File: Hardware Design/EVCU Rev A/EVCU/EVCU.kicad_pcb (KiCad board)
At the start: 4 copper layers, 119.4 x 76.4 mm, 89 parts, among them J1 Conn_01x06, J2 Conn_01x02, J3 APPS/BSE_Conn, J4 Micro_SD_Card, J5 DB9_Male, J6 Conn_01x02, Q1 Q_PMOS_GSD, U1 AZ1117-3.3, U10 EMIF06-MSD02N16, U11 ESDALC6V1W5, U2 AP62250WU-7, U3 STM32L4R9ZITx, U4 LM358, U5 MPU-6500, U6 SN65HVD230, U7 LM358, U9 ESDCAN24-2BLY, X1 ECS-2520MV-160-CN-TR

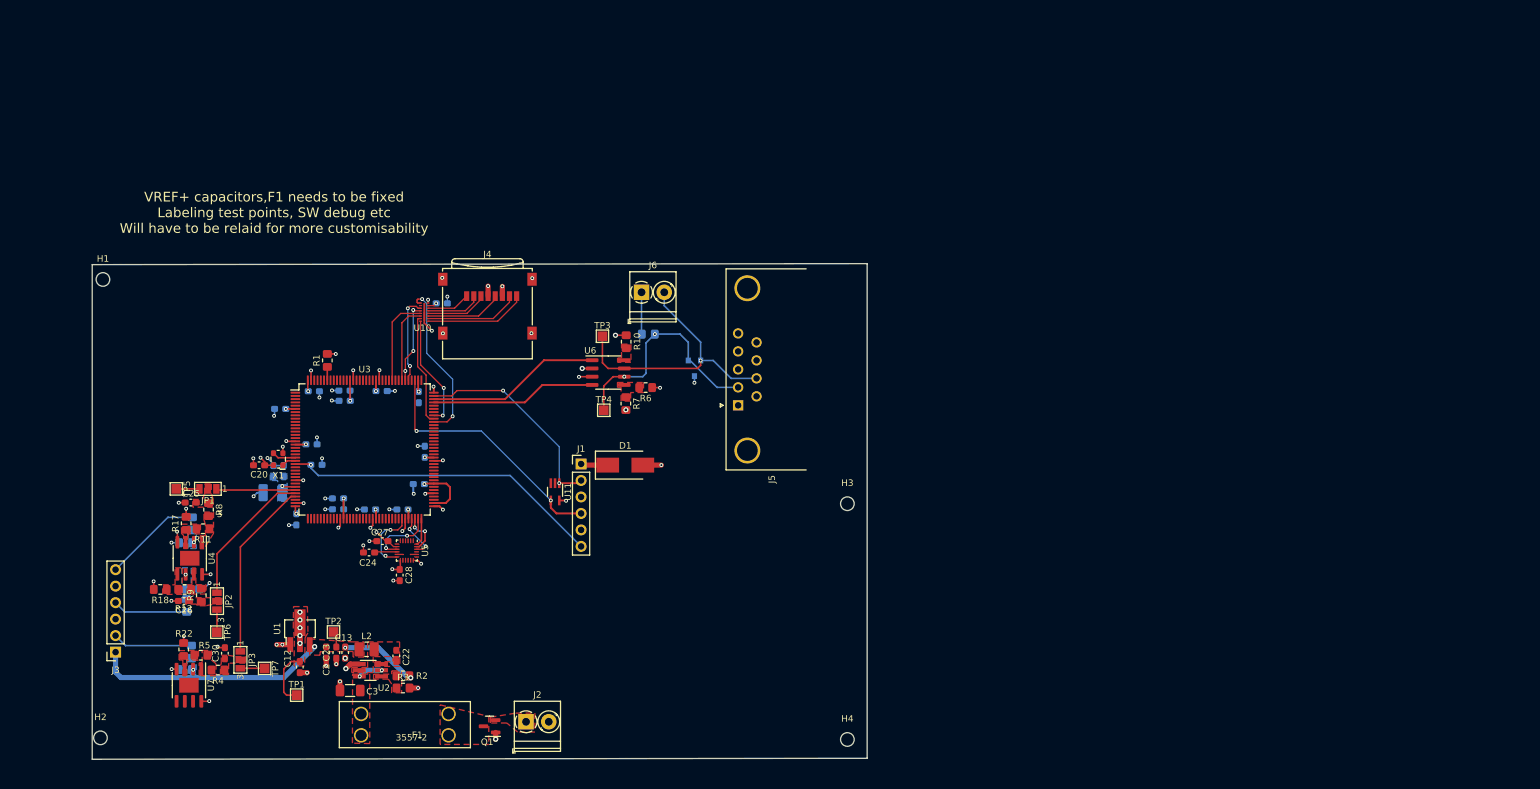
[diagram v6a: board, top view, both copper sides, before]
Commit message: silkscreen and drc clean up
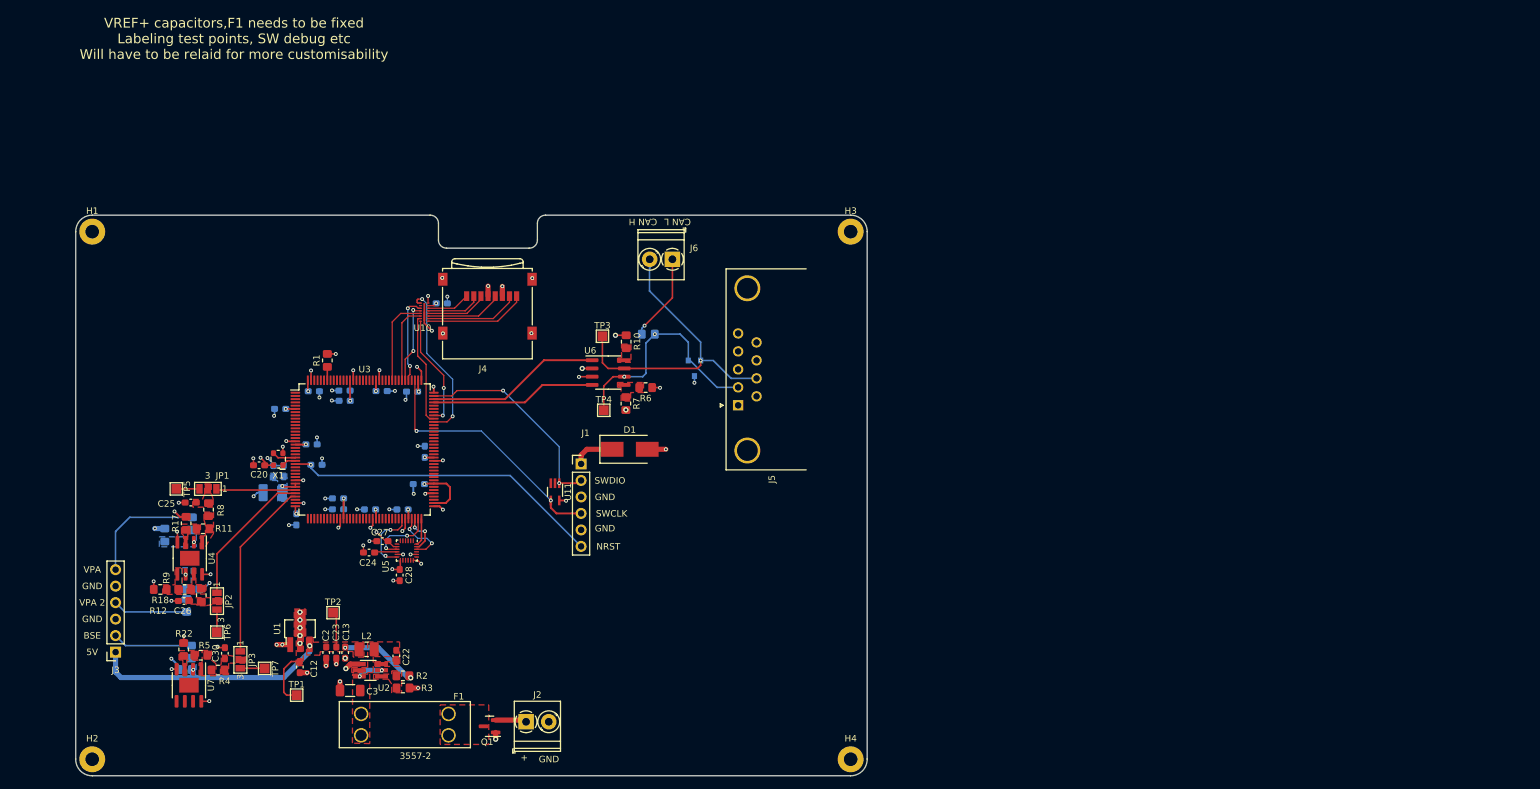
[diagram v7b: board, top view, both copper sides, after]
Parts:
- moved H3 41.9 mm to (132.1, 25.4)
- moved H1 7.55 mm to (15.2, 25.4)
- moved J6 6.96 mm to (104.6, 29.7), turned to 180 degrees
- moved H2 3.54 mm to (15.2, 106.7)
- moved R13 3.43 mm to (26.4, 72.1), turned to 90 degrees
- moved H4 3.09 mm to (132.1, 106.7)
- moved TP2 2.97 mm to (52.3, 84.1)
- moved D1 2.53 mm to (98.0, 58.9)
- moved C16 1.33 mm to (64.5, 50.0), turned to 180 degrees
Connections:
- F1 pad 1: (no net) -> Net-(F1-Pad)
- F1 pad 2: (no net) -> Net-(F1-Pad)
- F1 pad 3: (no net) -> +BATT
- F1 pad 4: (no net) -> +BATT
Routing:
- net Net-(J6-Pad1): track 6.47 -> 13.5 mm, vias 0 -> 1
- net GND: track 83.4 -> 90.3 mm, vias 66 -> 71
- net /CAN_H: track 43.1 -> 49.1 mm
- net Net-(J2-Pad1): track 0.00 -> 4.78 mm
- net /VPA: track 15.2 -> 18.6 mm
- net +3V3: track 59.3 -> 62.3 mm
- net +5V: track 50.6 -> 53.4 mm
- net /ACCEL_CS: track 6.98 -> 8.92 mm
- net +3.3VA: track 2.06 -> 2.56 mm
- net /MCU_DAT3: vias 3 -> 2
- removed copper zone on F.Cu, net Net-(J2-Pad1)
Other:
- board size 119.4 x 76.4 mm -> 121.9 x 86.4 mm
- board text added: "+"
- board text added: "5V"
- board text added: "BSE"
- board text added: "CAN H"
- board text added: "CAN L"
- board text added: "GND"
- board text added: "NRST"
- board text added: "SWCLK"
- board text added: "SWDIO"
- board text added: "VPA"
- board text added: "VPA 2"

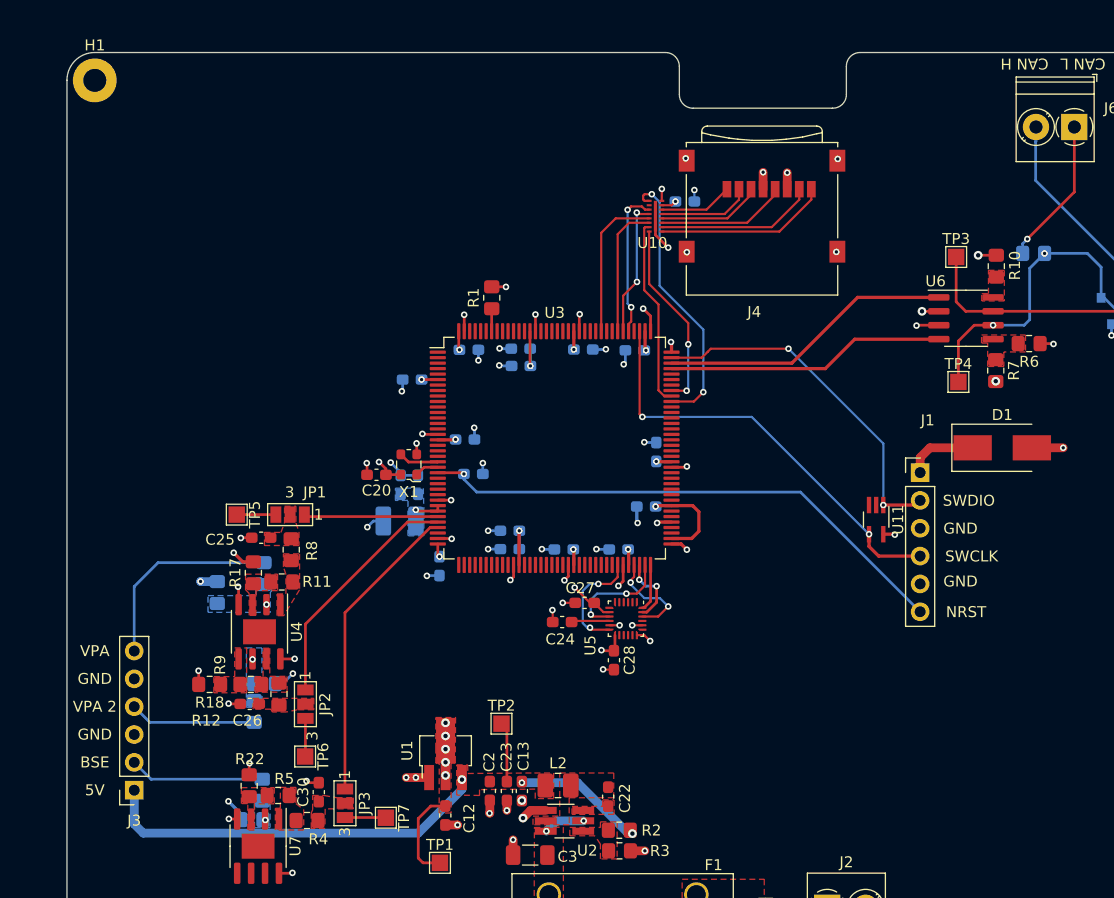
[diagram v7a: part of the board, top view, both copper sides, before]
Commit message: added vref+ caps, fixed f1 via error, fixed gyro footprint, pcb ready for manufacturing
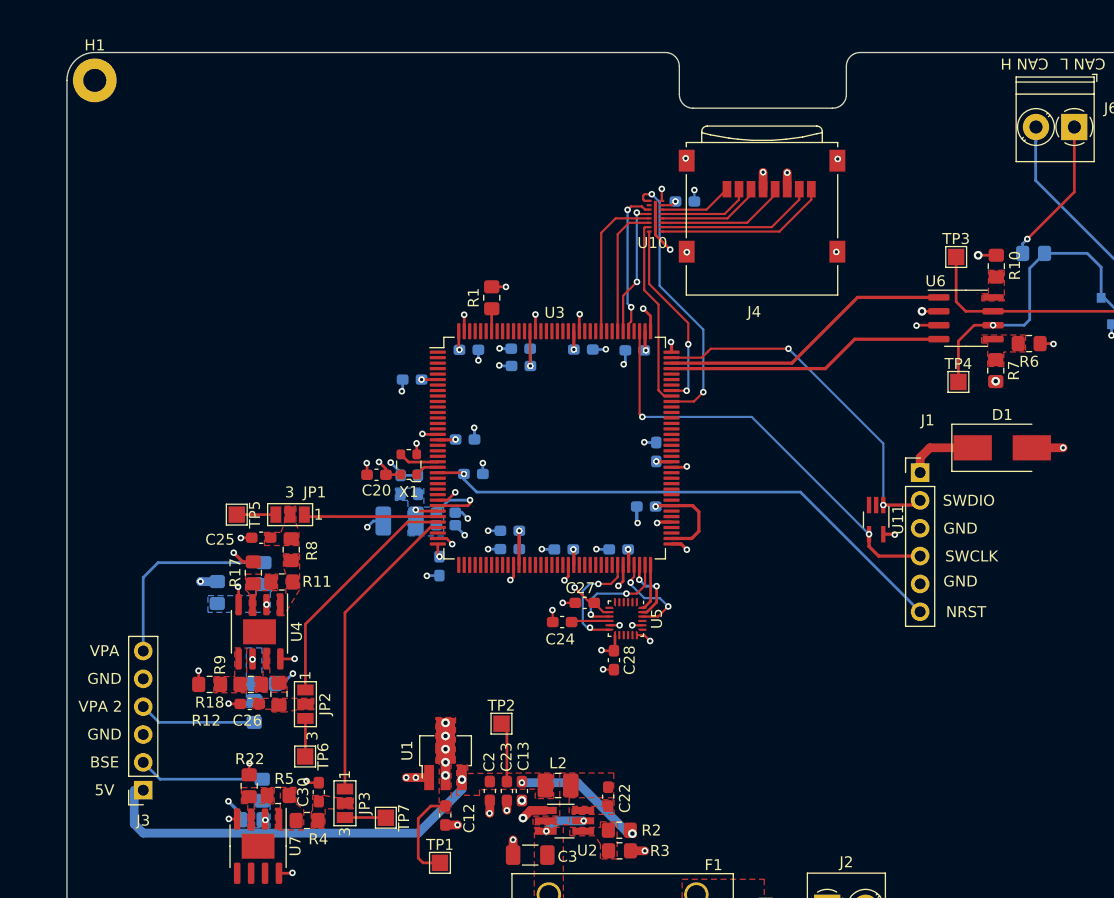
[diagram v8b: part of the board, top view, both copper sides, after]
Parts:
- added C32: 1uF, Capacitor_SMD:C_0603_1608Metric_Pad1.08x0.95mm_HandSolder, B.Cu at (47.3, 66.0)
- added C33: 100nF, Capacitor_SMD:C_0603_1608Metric_Pad1.08x0.95mm_HandSolder, B.Cu at (47.3, 64.8)
- U5: footprint Package_DFN_QFN:QFN-24-3x3mm_P0.4mm_EP1.75x1.6mm -> Package_DFN_QFN:QFN-24_3x3mm_P0.4mm
- moved J3 0.82 mm to (19.7, 90.2)
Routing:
- net +3.3VA: track 2.56 -> 8.93 mm, vias 1 -> 2
- net GND: track 90.3 -> 94.1 mm, vias 71 -> 73
- net /VPA_BSE: track 12.3 -> 11.5 mm
- net /VPA_2: track 11.5 -> 10.7 mm
- net /CAN_L: vias 2 -> 1
